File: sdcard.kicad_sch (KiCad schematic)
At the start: 20 parts, among them J7 microSD push-pull, Q2 -20V 2.3A P-ch, Q3 60V 300mA N-ch

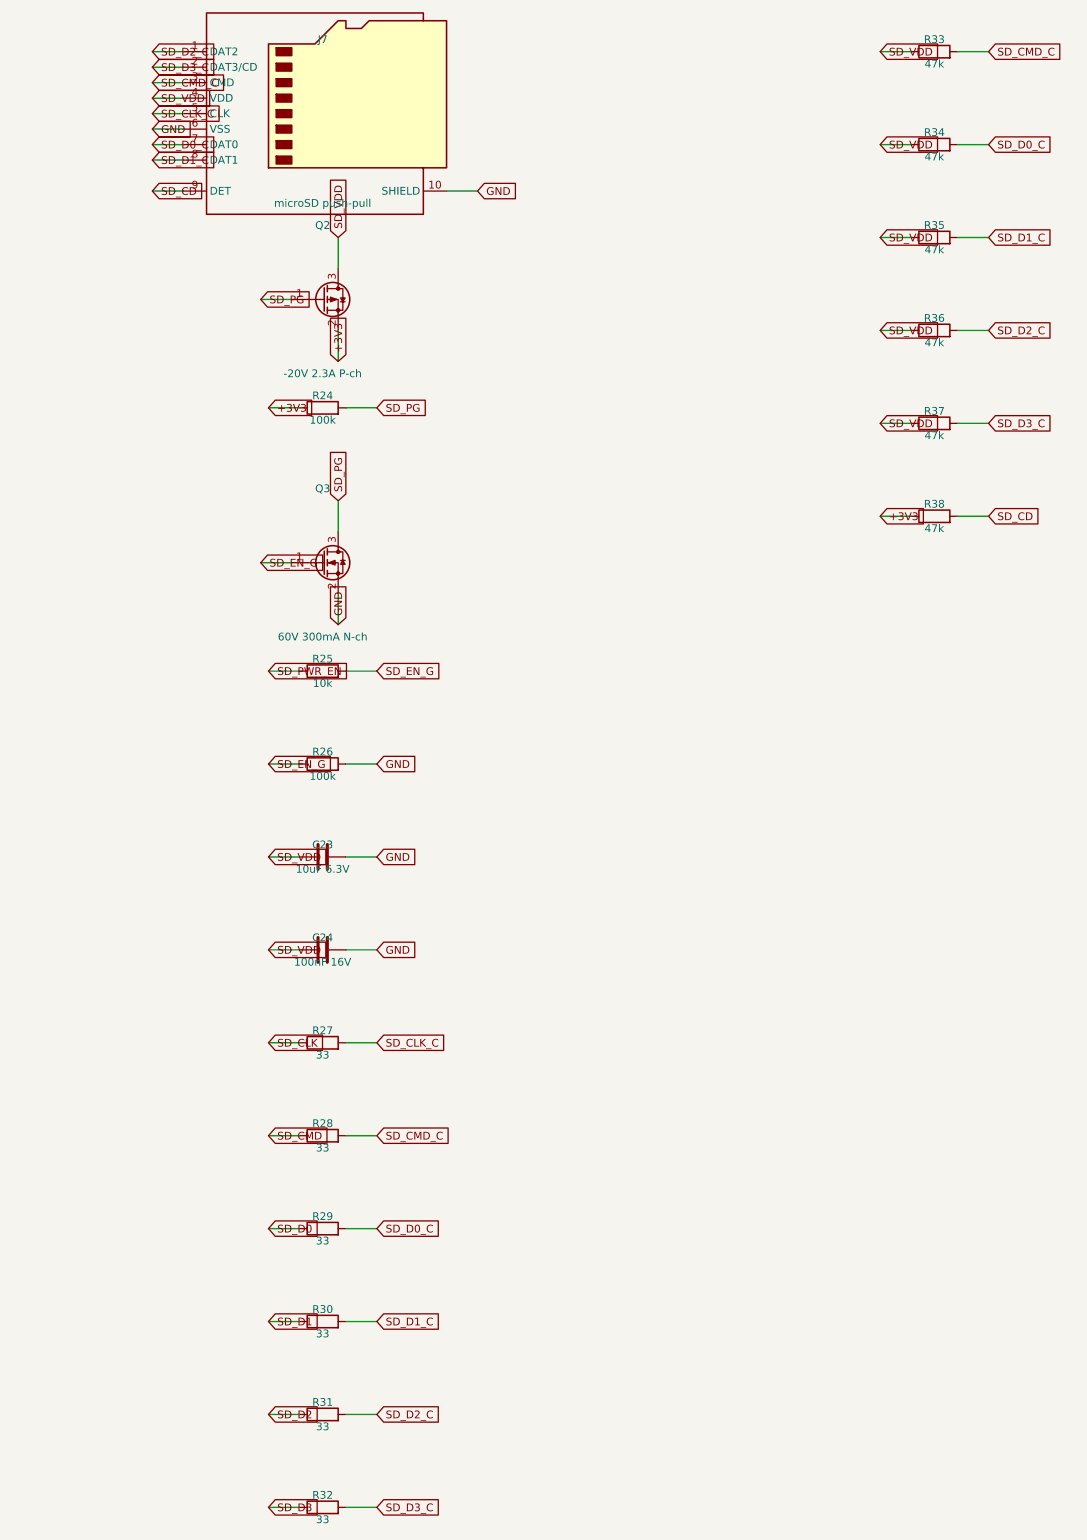
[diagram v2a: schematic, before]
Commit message: Add WS2812 5V DIN, SPI breakout, and PCB handoff docs.
Shift-light header uses a 74AHCT1G125 so GPIO48 drives real 5V data; SPI lands on IO40/41/42/47 with spare IO3/45/46 kept. README §10 covers remaining routing for the next agent.

Co-authored-by: Cursor <cursoragent@cursor.com>
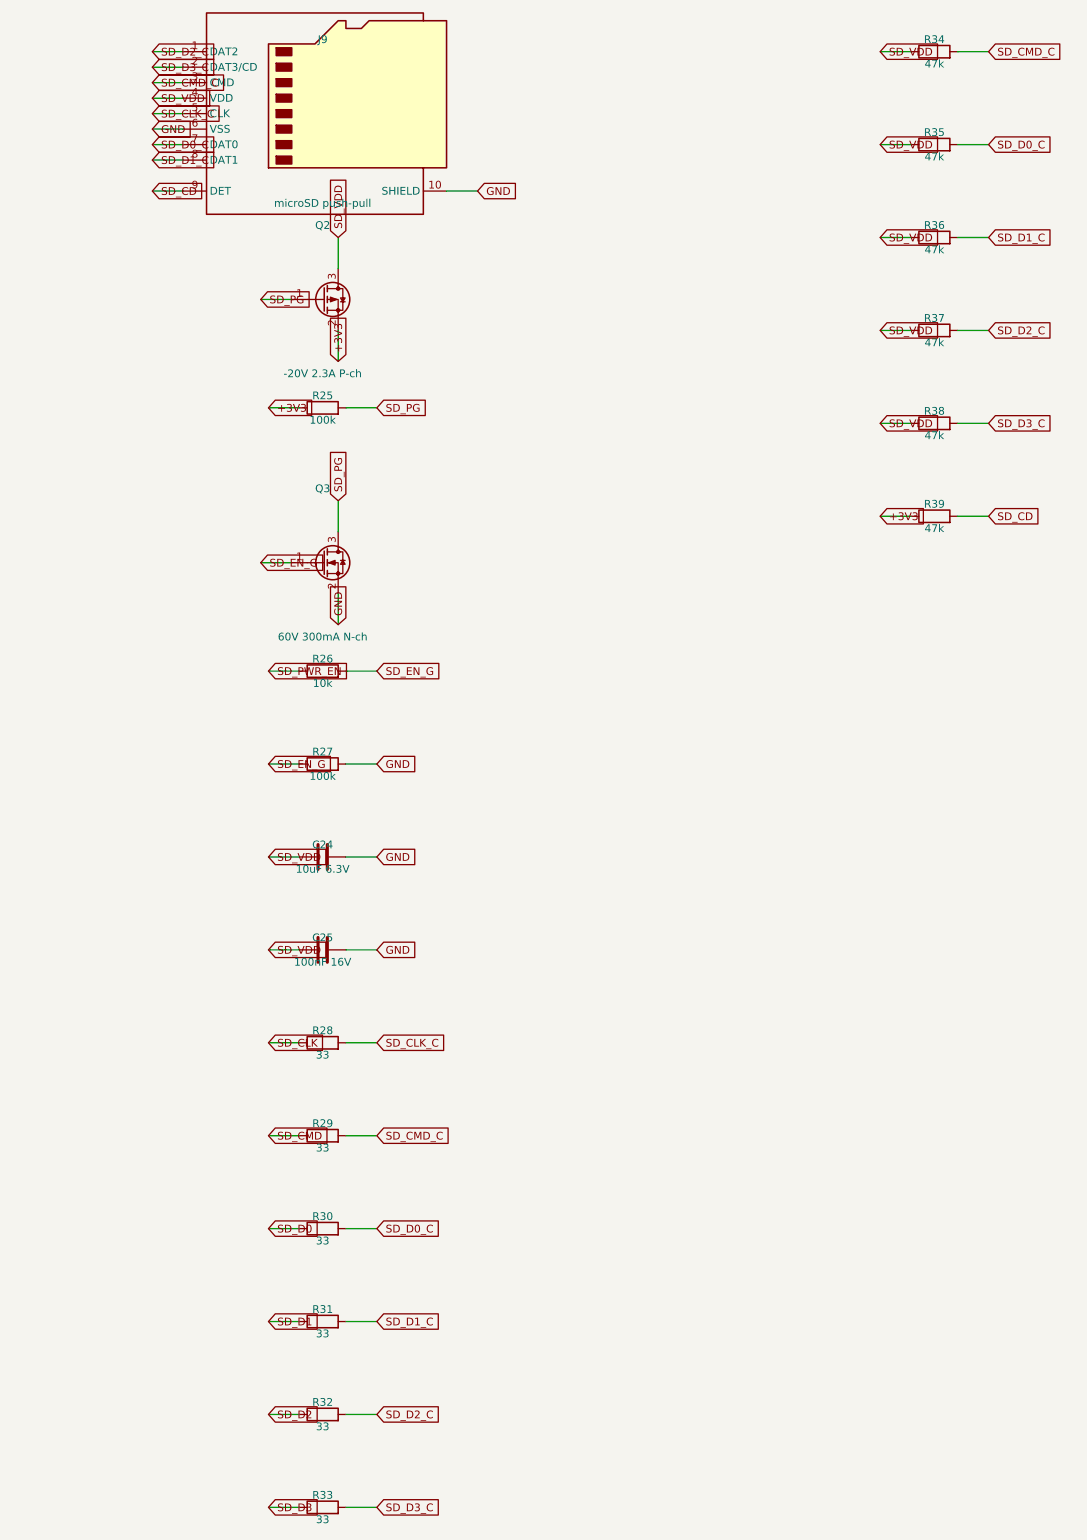
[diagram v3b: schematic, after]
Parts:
- removed C23: 10uF 6.3V, Capacitor_SMD:C_1206_3216Metric, symbol Device:C
- removed J7: microSD push-pull, Connector_Card:microSD_HC_Hirose_DM3D-SF, symbol Connector:Micro_SD_Card_Det1
- removed R24: 100k, Resistor_SMD:R_0805_2012Metric, symbol Device:R
- added C25: 100nF 16V, Capacitor_SMD:C_0805_2012Metric, symbol Device:C
- added J9: microSD push-pull, Connector_Card:microSD_HC_Hirose_DM3D-SF, symbol Connector:Micro_SD_Card_Det1
- added R39: 47k, Resistor_SMD:R_0805_2012Metric, symbol Device:R
- C24: value 100nF 16V -> 10uF 6.3V; footprint Capacitor_SMD:C_0805_2012Metric -> Capacitor_SMD:C_1206_3216Metric
- R25: value 10k -> 100k; Note (none) -> Default off
- R26: value 100k -> 10k
- R27: value 33 -> 100k; Note Series damping -> (none)
- R33: value 47k -> 33; Note Pulled to the switched rail so nothing back-feeds a powered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 -> Series damping
- R38: Note Card-detect pull-up -> Pulled to the switched rail so nothing back-feeds a powered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
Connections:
- net +3V3: now also R25.1, R39.1; no longer R38.1
- net GND: now also R27.2, C25.2, J9.10 (SHIELD), J9.6 (VSS); no longer R26.2
- net SD_CD: now also J9.9 (DET), R39.2; no longer R38.2
- net SD_CLK: now also R28.1; no longer R27.1
- net SD_CLK_C: now also R28.2, J9.5 (CLK); no longer R27.2
- net SD_CMD: now also R29.1; no longer R28.1
- net SD_CMD_C: now also R29.2, R34.2, J9.3 (CMD); no longer R28.2, R33.2
- net SD_D0: now also R30.1; no longer R29.1
- net SD_D0_C: now also R30.2, R35.2, J9.7 (DAT0); no longer R29.2, R34.2
- net SD_D1: now also R31.1; no longer R30.1
- net SD_D1_C: now also R31.2, R36.2, J9.8 (DAT1); no longer R30.2, R35.2
- net SD_D2: now also R32.1; no longer R31.1
- net SD_D2_C: now also R32.2, R37.2, J9.1 (DAT2); no longer R31.2, R36.2
- net SD_D3: now also R33.1; no longer R32.1
- net SD_D3_C: now also R33.2, R38.2, J9.2 (DAT3/CD); no longer R32.2, R37.2
- net SD_EN_G: now also R26.2, R27.1; no longer R25.2, R26.1
- net SD_PG: now also R25.2
- net SD_PWR_EN: now also R26.1; no longer R25.1
- net SD_VDD: now also R38.1, C25.1, J9.4 (VDD); no longer R33.1
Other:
- moved on the sheet: C24, R25, R26, R27, R28, R29, R30, R31, R32, R33, R34, R35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

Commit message: Fix netclasses being silently lost: the power rails were 0.2 mm
Checking the ESP32 pin assignments turned up something worse than a pin
conflict. The committed project file held only the Default netclass and
zero netclass patterns, so Power (0.5 mm track, 0.8 mm via) and CAN had
never been applied and the whole board routed at 0.2 mm -- including +5V
and +5VS, which are 1 A rails.

Nothing caught it because narrow track is legal track. 0.2 mm in 1 oz
copper is 1.01 A at a 20 C rise and drops 147 mV over a 60 mm run; on
+5VS, the sensor excitation rail, that droop lands straight on every
ratiometric reading the 0.1% dividers and the 16-bit ADC exist to
protect.

Three separate causes, all fixed:

  - generate_pcb.py builds its board with CreateEmptyBoard(), which knows
    only the Default class, and saving it rewrote the .kicad_pro from the
    board's own settings. It now lifts net_settings out before the save
    and restores it after, and says what it restored.

  - maze_route.py and finish_routing.py hardcoded 0.2 mm for their
    fix-up traces, so +5VS came back 58 mm at the correct 0.5 mm and
    89 mm at 0.2. Both now size tracks and vias per net through the new
    gen/netclasses.py, which reads the classes and their glob patterns
    from the project file -- net.GetNetClass() hands back an undecorated
    SwigPyObject here, and a try/except around it is exactly how a
    default silently becomes a power rail.

  - The min-drill rule (0.2 mm, needed by the LM5164 thermal vias) lived
    only in the board object, so regenerating the schematic reset it to
    0.3 and made those vias illegal. It is in the project template now,
    so it survives in either order.

Also fixed, found while re-routing: the island builder rasterised pads
from their bounding boxes, but a 1.70 mm round header pad's bounding box
corners are ~0.35 mm off the copper, so 23% of the apparent landing area
is bare laminate. Routes ended there, connected nothing, and the router
then called th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
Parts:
- R34, R35, R36, R37, R38: value 47k -> 10k; Note Pulled to the switched rail so nothing back-feeds a powered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 -> Espressif's recommended value; pulled to the switched rail 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
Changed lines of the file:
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@@
       (effects (font (size 1.27 1.27)) )
     )
-    (property "Value" "47k" (at 170.18 19.78 270)
+    (property "Value" "10k" (at 170.18 19.78 270)
       (effects (font (size 1.27 1.27)) )
     )
@@
       (effects (font (size 1.27 1.27)) hide)
     )
-    (property "Note" "Pulled to the switched rail so nothing back-feeds a powered-down card" (at 170.18 19.78 270)
+    (property "Note" "Espressif's recommended value; pulled to the switched rail so nothing back-feeds a powered-down card" (at 170.18 19.78 270)
       (effects (font (size 1.27 1.27)) hide)
     )
@@
       (effects (font (size 1.27 1.27)) )
     )
-    (property "Value" "47k" (at 170.18 35.02 270)
+    (property "Value" "10k" (at 170.18 35.02 270)
       (effects (font (size 1.27 1.27)) )
     )
@@
       (effects (font (size 1.27 1.27)) hide)
     )
-    (property "Note" "Pulled to the switched rail so nothing back-feeds a powered-down card" (at 170.18 35.02 270)
+    (property "Note" "Espressif's recommended value; pulled to the switched rail so nothing back-feeds a powered-down card" (at 170.18 35.02 270)
       (effects (font (size 1.27 1.27)) hide)
     )
@@
       (effects (font (size 1.27 1.27)) )
     )
-    (property "Value" "47k" (at 170.18 50.26 270)
+    (property "Value" "10k" (at 170.18 50.26 270)
       (effects (font (size 1.27 1.27)) )
     )
@@
       (effects (font (size 1.27 1.27)) hide)
     )
-    (property "Note" "Pulled to the switched rail so nothing back-feeds a powered-down card" (at 170.18 50.26 270)
+    (property "Note" "Espressif's recommended value; pulled to the switched rail so nothing back-feeds a powered-down card" (at 170.18 50.26 270)
       (effects (font (size 1.27 1.27)) hide)
     )
@@
       (effects (font (size 1.27 1.27)) )
     )
-    (property "Value" "47k" (at 170.18 65.5 270)
+    (property "Value" "10k" (at 170.18 65.5 270)
       (effects (font (size 1.27 1.27)) )
     )
@@
       (effects (font (size 1.27 1.27)) hide)
     )
-    (property "Note" "Pulled to the switched rail so nothing back-feeds a powered-down card" (at 170.18 65.5 270)
+    (property "Note" "Espressif's recommended value; pulled to the switched rail so nothing back-feeds a powered-down card" (at 170.18 65.5 270)
       (effects (font (size 1.27 1.27)) hide)
     )
@@
       (effects (font (size 1.27 1.27)) )
     )
-    (property "Value" "47k" (at 170.18 80.74 270)
+    (property "Value" "10k" (at 170.18 80.74 270)
       (effects (font (size 1.27 1.27)) )
     )
@@
       (effects (font (size 1.27 1.27)) hide)
     )
-    (property "Note" "Pulled to the switched rail so nothing back-feeds a powered-down card" (at 170.18 80.74 270)
+    (property "Note" "Espressif's recommended value; pulled to the switched rail so nothing back-feeds a powered-down card" (at 170.18 80.74 270)
       (effects (font (size 1.27 1.27)) hide)
     )
